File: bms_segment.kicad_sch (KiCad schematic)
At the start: 103 parts, among them J1 Conn_02x09_Counter_Clockwise, J2 Conn_02x09_Counter_Clockwise, J5 Conn_01x04, J6 Conn_01x04, J7 Conn_01x06, SW1 SW_Push, U1 LMR516xx, U2 MAX14921, U3 MAX11163, U4 REF61xx, U5 STM32F103C8Tx, U6 ADuM1252

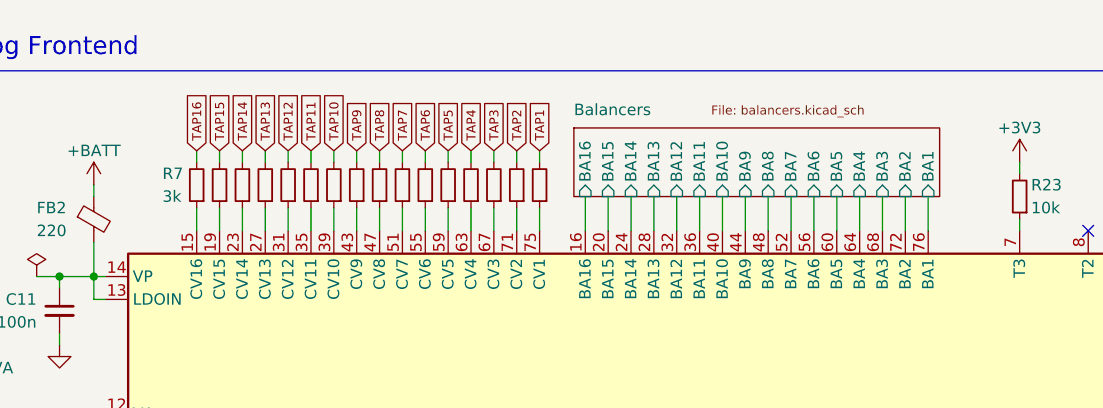
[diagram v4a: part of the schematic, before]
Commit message: schematic: Use resistor arrays for 3k resistors
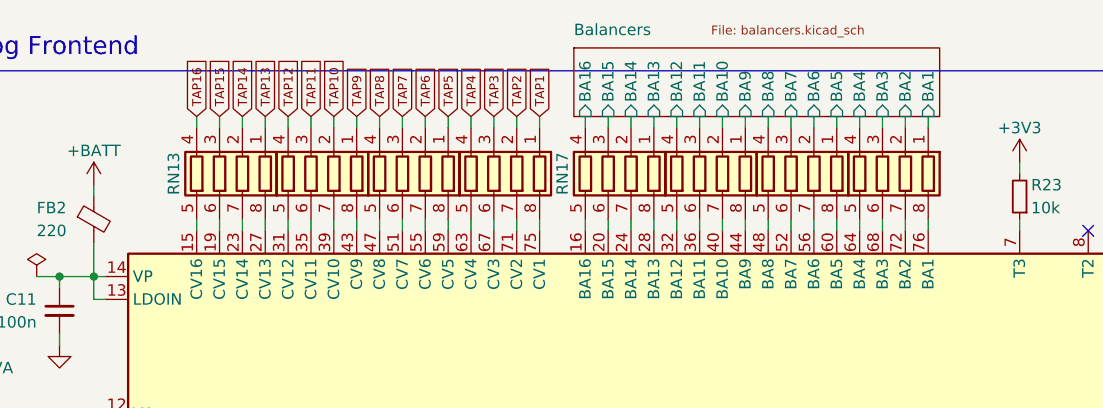
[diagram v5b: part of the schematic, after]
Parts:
- removed R10, R11, R12, R13, R14, R15, R16, R17, R18, R19, R20, R21, R22, R7, R8, R9: 3k, Resistor_SMD:R_0603_1608Metric, symbol Device:R_Small
- added RN13, RN14, RN15, RN16, RN17, RN18, RN19, RN20: 3k, Resistor_SMD:R_Array_Concave_4x0603, symbol Device:R_Pack04
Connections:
- net Balancers/BA1: now also RN20.1 (R1.1); no longer U2.76 (BA1)
- net Balancers/BA10: now also RN18.2 (R2.1); no longer U2.40 (BA10)
- net Balancers/BA11: now also RN18.3 (R3.1); no longer U2.36 (BA11)
- net Balancers/BA12: now also RN18.4 (R4.1); no longer U2.32 (BA12)
- net Balancers/BA13: now also RN17.1 (R1.1); no longer U2.28 (BA13)
- net Balancers/BA14: now also RN17.2 (R2.1); no longer U2.24 (BA14)
- net Balancers/BA15: now also RN17.3 (R3.1); no longer U2.20 (BA15)
- net Balancers/BA16: now also RN17.4 (R4.1); no longer U2.16 (BA16)
- net Balancers/BA2: now also RN20.2 (R2.1); no longer U2.72 (BA2)
- net Balancers/BA3: now also RN20.3 (R3.1); no longer U2.68 (BA3)
- net Balancers/BA4: now also RN20.4 (R4.1); no longer U2.64 (BA4)
- net Balancers/BA5: now also RN19.1 (R1.1); no longer U2.60 (BA5)
- net Balancers/BA6: now also RN19.2 (R2.1); no longer U2.56 (BA6)
- net Balancers/BA7: now also RN19.3 (R3.1); no longer U2.52 (BA7)
- net Balancers/BA8: now also RN19.4 (R4.1); no longer U2.48 (BA8)
- net Balancers/BA9: now also RN18.1 (R1.1); no longer U2.44 (BA9)
- net TAP1: now also RN16.1 (R1.1)
- net TAP10: now also RN14.2 (R2.1)
- net TAP11: now also RN14.3 (R3.1)
- net TAP12: now also RN14.4 (R4.1)
- net TAP13: now also RN13.1 (R1.1)
- net TAP14: now also RN13.2 (R2.1)
- net TAP15: now also RN13.3 (R3.1)
- net TAP16: now also RN13.4 (R4.1)
- net TAP2: now also RN16.2 (R2.1)
- net TAP3: now also RN16.3 (R3.1)
- net TAP4: now also RN16.4 (R4.1)
- net TAP5: now also RN15.1 (R1.1)
- net TAP6: now also RN15.2 (R2.1)
- net TAP7: now also RN15.3 (R3.1)
- net TAP8: now also RN15.4 (R4.1)
- net TAP9: now also RN14.1 (R1.1)
- net at U2.71 (CV2): now also RN16.7 (R2.2)
- net at U2.43 (CV9): now also RN14.8 (R1.2)
- net at U2.15 (CV16): now also RN13.5 (R4.2)
- net at U2.19 (CV15): now also RN13.6 (R3.2)
- net at U2.23 (CV14): now also RN13.7 (R2.2)
- net at U2.27 (CV13): now also RN13.8 (R1.2)
- net at U2.31 (CV12): now also RN14.5 (R4.2)
- net at U2.35 (CV11): now also RN14.6 (R3.2)
- net at U2.39 (CV10): now also RN14.7 (R2.2)
- net at U2.47 (CV8): now also RN15.5 (R4.2)
- net at U2.51 (CV7): now also RN15.6 (R3.2)
- net at U2.55 (CV6): now also RN15.7 (R2.2)
- net at U2.59 (CV5): now also RN15.8 (R1.2)
- net at U2.63 (CV4): now also RN16.5 (R4.2)
- net at U2.67 (CV3): now also RN16.6 (R3.2)
- net at U2.75 (CV1): now also RN16.8 (R1.2)
- new net: RN17.5 (R4.2), U2.16 (BA16)
- new net: RN17.6 (R3.2), U2.20 (BA15)
- new net: RN17.7 (R2.2), U2.24 (BA14)
- new net: RN17.8 (R1.2), U2.28 (BA13)
- new net: RN18.5 (R4.2), U2.32 (BA12)
- new net: RN18.6 (R3.2), U2.36 (BA11)
- new net: RN18.7 (R2.2), U2.40 (BA10)
- new net: RN18.8 (R1.2), U2.44 (BA9)
- new net: RN19.5 (R4.2), U2.48 (BA8)
- new net: RN19.6 (R3.2), U2.52 (BA7)
- new net: RN19.7 (R2.2), U2.56 (BA6)
- new net: RN19.8 (R1.2), U2.60 (BA5)
- new net: RN20.5 (R4.2), U2.64 (BA4)
- new net: RN20.6 (R3.2), U2.68 (BA3)
- new net: RN20.7 (R2.2), U2.72 (BA2)
- new net: RN20.8 (R1.2), U2.76 (BA1)

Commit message: Revision E
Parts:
- removed J1, J2: Conn_02x09_Counter_Clockwise, yfs:MolexMilliGrid2x9, symbol Connector_Generic:Conn_02x09_Counter_Clockwise
- added HS1: Heatsink, TestPoint:TestPoint_Pad_D1.0mm, symbol Mechanical:Heatsink
- added HS2: PLACEHOLDER, TestPoint:TestPoint_Pad_D1.0mm, symbol Mechanical:Heatsink
- added J10: Conn_02x17_Counter_Clockwise, yfs:SAMTEC_TW-17-03-F-D-275-090, symbol Connector_Generic:Conn_02x17_Counter_Clockwise
- J5, J6: footprint Connector_JST:JST_PH_B4B-PH-K_1x04_P2.00mm_Vertical -> yfs:MolexMicrofitPlus2x2-RA
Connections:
- net Balancers/BA1: now also RN20.8 (R1.2); no longer RN20.1 (R1.1)
- net Balancers/BA10: now also RN16.6 (R3.2); no longer RN18.2 (R2.1)
- net Balancers/BA11: now also RN15.8 (R1.2); no longer RN18.3 (R3.1)
- net Balancers/BA12: now also RN15.6 (R3.2); no longer RN18.4 (R4.1)
- net Balancers/BA13: now also RN14.8 (R1.2); no longer RN17.1 (R1.1)
- net Balancers/BA14: now also RN14.6 (R3.2); no longer RN17.2 (R2.1)
- net Balancers/BA15: now also RN13.8 (R1.2); no longer RN17.3 (R3.1)
- net Balancers/BA16: now also RN13.6 (R3.2); no longer RN17.4 (R4.1)
- net Balancers/BA2: now also RN20.6 (R3.2); no longer RN20.2 (R2.1)
- net Balancers/BA3: now also RN19.8 (R1.2); no longer RN20.3 (R3.1)
- net Balancers/BA4: now also RN19.6 (R3.2); no longer RN20.4 (R4.1)
- net Balancers/BA5: now also RN18.8 (R1.2); no longer RN19.1 (R1.1)
- net Balancers/BA6: now also RN18.6 (R3.2); no longer RN19.2 (R2.1)
- net Balancers/BA7: now also RN17.8 (R1.2); no longer RN19.3 (R3.1)
- net Balancers/BA8: now also RN17.6 (R3.2); no longer RN19.4 (R4.1)
- net Balancers/BA9: now also RN16.8 (R1.2); no longer RN18.1 (R1.1)
- net GND: now also J10.1 (Pin_1), J10.2 (Pin_2)
- net TAP1: now also RN20.7 (R2.2), J10.3 (Pin_3), J10.4 (Pin_4); no longer RN16.1 (R1.1)
- net TAP10: now also RN16.5 (R4.2), J10.21 (Pin_21), J10.22 (Pin_22); no longer RN14.2 (R2.1)
- net TAP11: now also RN15.7 (R2.2), J10.23 (Pin_23), J10.24 (Pin_24); no longer RN14.3 (R3.1)
- net TAP12: now also RN15.5 (R4.2), J10.25 (Pin_25), J10.26 (Pin_26); no longer RN14.4 (R4.1)
- net TAP13: now also RN14.7 (R2.2), J10.27 (Pin_27), J10.28 (Pin_28); no longer RN13.1 (R1.1)
- net TAP14: now also RN14.5 (R4.2), J10.29 (Pin_29), J10.30 (Pin_30); no longer RN13.2 (R2.1)
- net TAP15: now also RN13.7 (R2.2), J10.31 (Pin_31), J10.32 (Pin_32); no longer RN13.3 (R3.1)
- net TAP16: now also RN13.5 (R4.2), J10.33 (Pin_33), J10.34 (Pin_34); no longer RN13.4 (R4.1)
- net TAP2: now also RN20.5 (R4.2), J10.5 (Pin_5), J10.6 (Pin_6); no longer RN16.2 (R2.1)
- net TAP3: now also RN19.7 (R2.2), J10.7 (Pin_7), J10.8 (Pin_8); no longer RN16.3 (R3.1)
- net TAP4: now also RN19.5 (R4.2), J10.10 (Pin_10), J10.9 (Pin_9); no longer RN16.4 (R4.1)
- net TAP5: now also RN18.7 (R2.2), J10.11 (Pin_11), J10.12 (Pin_12); no longer RN15.1 (R1.1)
- net TAP6: now also RN18.5 (R4.2), J10.13 (Pin_13), J10.14 (Pin_14); no longer RN15.2 (R2.1)
- net TAP7: now also RN17.7 (R2.2), J10.15 (Pin_15), J10.16 (Pin_16); no longer RN15.3 (R3.1)
- net TAP8: now also RN17.5 (R4.2), J10.17 (Pin_17), J10.18 (Pin_18); no longer RN15.4 (R4.1)
- net TAP9: now also RN16.7 (R2.2), J10.19 (Pin_19), J10.20 (Pin_20); no longer RN14.1 (R1.1)
- net CV12: now reaches U2.31 (CV12)
- net CV12: now also RN15.4 (R4.1); no longer RN14.5 (R4.2)
- net CV11: now reaches U2.35 (CV11)
- net CV11: now also RN15.2 (R2.1); no longer RN14.6 (R3.2)
- net CV10: now reaches U2.39 (CV10)
- net CV10: now also RN16.4 (R4.1); no longer RN14.7 (R2.2)
- net CV9: now reaches U2.43 (CV9)
- net CV9: now also RN16.2 (R2.1); no longer RN14.8 (R1.2)
- net CV4: now reaches U2.63 (CV4)
- net CV4: now also RN19.4 (R4.1); no longer RN16.5 (R4.2)
- net CV3: now reaches U2.67 (CV3)
- net CV3: now also RN19.2 (R2.1); no longer RN16.6 (R3.2)
- net CV2: now reaches U2.71 (CV2)
- net CV2: now also RN20.4 (R4.1); no longer RN16.7 (R2.2)
- net CV1: now reaches U2.75 (CV1)
- net CV1: now also RN20.2 (R2.1); no longer RN16.8 (R1.2)
- net CV16: now reaches U2.15 (CV16)
- net CV16: now also RN13.4 (R4.1); no longer RN13.5 (R4.2)
- net CV15: now reaches U2.19 (CV15)
- net CV15: now also RN13.2 (R2.1); no longer RN13.6 (R3.2)
- net CV14: now reaches U2.23 (CV14)
- net CV14: now also RN14.4 (R4.1); no longer RN13.7 (R2.2)
- net CV13: now reaches U2.27 (CV13)
- net CV13: now also RN14.2 (R2.1); no longer RN13.8 (R1.2)
- net BA16: now reaches U2.16 (BA16)
- net BA16: now also RN13.3 (R3.1); no longer RN17.5 (R4.2)
- net at U2.17 (CT16): now also C12.1; no longer C12.2
- net at U2.18 (CB16): now also C12.2; no longer C12.1
- net BA15: now reaches U2.20 (BA15)
- net BA15: now also RN13.1 (R1.1); no longer RN17.6 (R3.2)
- net BA14: now reaches U2.24 (BA14)
- net BA14: now also RN14.3 (R3.1); no longer RN17.7 (R2.2)
- net BA13: now reaches U2.28 (BA13)
- net BA13: now also RN14.1 (R1.1); no longer RN17.8 (R1.2)
- net BA12: now reaches U2.32 (BA12)
- net BA12: now also RN15.3 (R3.1); no longer RN18.5 (R4.2)
- net BA11: now reaches U2.36 (BA11)
- net BA11: now also RN15.1 (R1.1); no longer RN18.6 (R3.2)
- net BA10: now reaches U2.40 (BA10)
- net BA10: now also RN16.3 (R3.1); no longer RN18.7 (R2.2)
- net BA9: now reaches U2.44 (BA9)
- net BA9: now also RN16.1 (R1.1); no longer RN18.8 (R1.2)
- net CV8: now reaches U2.47 (CV8)
- net CV8: now also RN17.4 (R4.1); no longer RN15.5 (R4.2)
- net BA8: now reaches U2.48 (BA8)
- net BA8: now also RN17.3 (R3.1); no longer RN19.5 (R4.2)
- net CV7: now reaches U2.51 (CV7)
- net CV7: now also RN17.2 (R2.1); no longer RN15.6 (R3.2)
- net BA7: now reaches U2.52 (BA7)
- net BA7: now also RN17.1 (R1.1); no longer RN19.6 (R3.2)
- net CV6: now reaches U2.55 (CV6)
- net CV6: now also RN18.4 (R4.1); no longer RN15.7 (R2.2)
- net BA6: now reaches U2.56 (BA6)
- net BA6: now also RN18.3 (R3.1); no longer RN19.7 (R2.2)
- net CV5: now reaches U2.59 (CV5)
- net CV5: now also RN18.2 (R2.1); no longer RN15.8 (R1.2)
- net BA5: now reaches U2.60 (BA5)
- net BA5: now also RN18.1 (R1.1); no longer RN19.8 (R1.2)
- net BA4: now reaches U2.64 (BA4)
- net BA4: now also RN19.3 (R3.1); no longer RN20.5 (R4.2)
- net BA3: now reaches U2.68 (BA3)
- net BA3: now also RN19.1 (R1.1); no longer RN20.6 (R3.2)
- net BA2: now reaches U2.72 (BA2)
- net BA2: now also RN20.3 (R3.1); no longer RN20.7 (R2.2)
- net BA1: now reaches U2.76 (BA1)
- net BA1: now also RN20.1 (R1.1); no longer RN20.8 (R1.2)
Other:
- moved on the sheet: C12, RN13

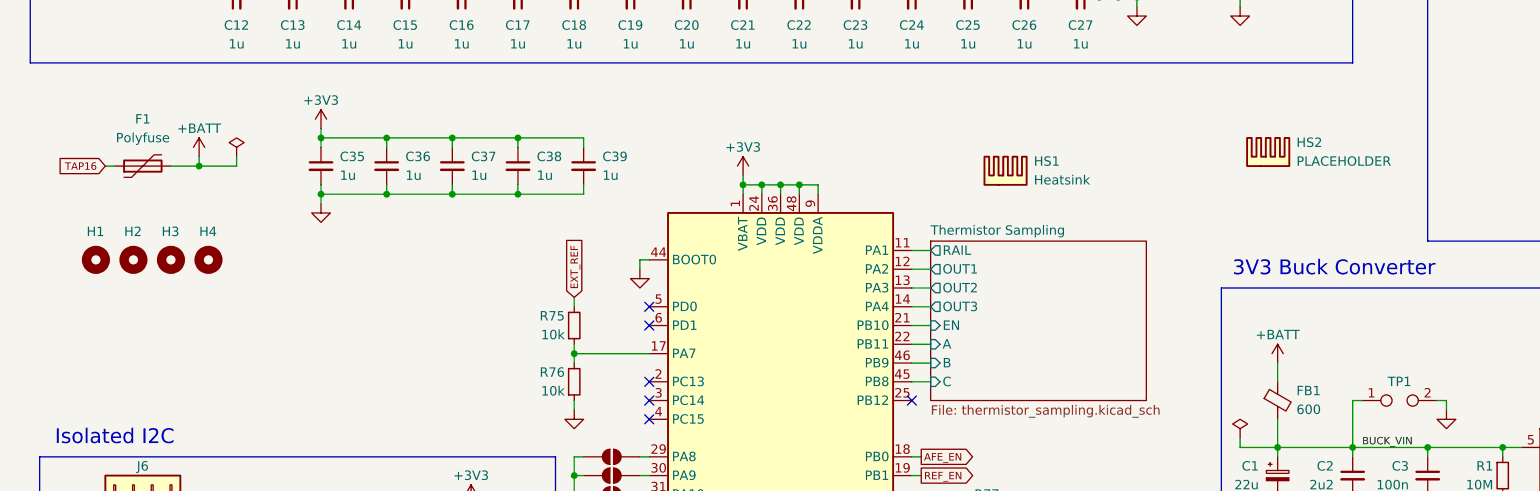
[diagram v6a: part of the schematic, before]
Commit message: Passing DRC & stacking stripes
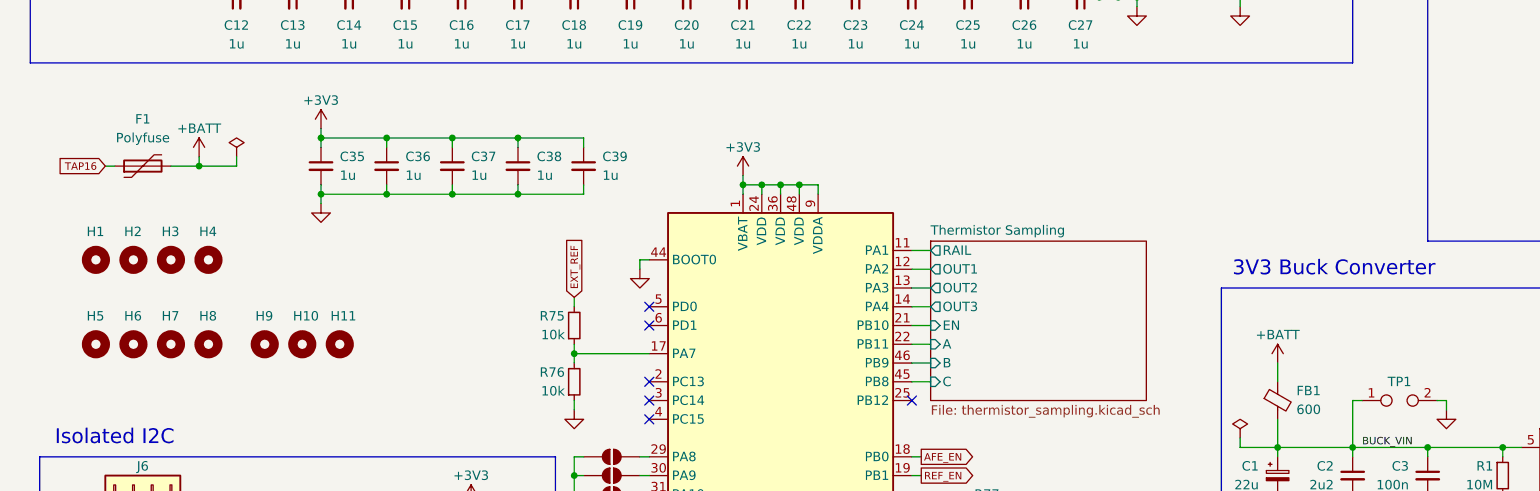
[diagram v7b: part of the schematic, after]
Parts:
- removed HS1: Heatsink, TestPoint:TestPoint_Pad_D1.0mm, symbol Mechanical:Heatsink
- removed HS2: PLACEHOLDER, TestPoint:TestPoint_Pad_D1.0mm, symbol Mechanical:Heatsink
- added H10, H11, H5, H6, H7, H8, H9: MountingHole, MountingHole:MountingHole_3.2mm_M3, symbol Mechanical:MountingHole

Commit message: *: Minor cleanup
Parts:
- renumbered J10 to J1, J5 to J4, J6 to J5
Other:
- moved on the sheet: J1
